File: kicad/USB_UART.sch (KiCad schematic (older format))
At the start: 10 parts, among them J3 USB-Micro, P5 CONN_1, P6 CONN_1, U3 CP210X

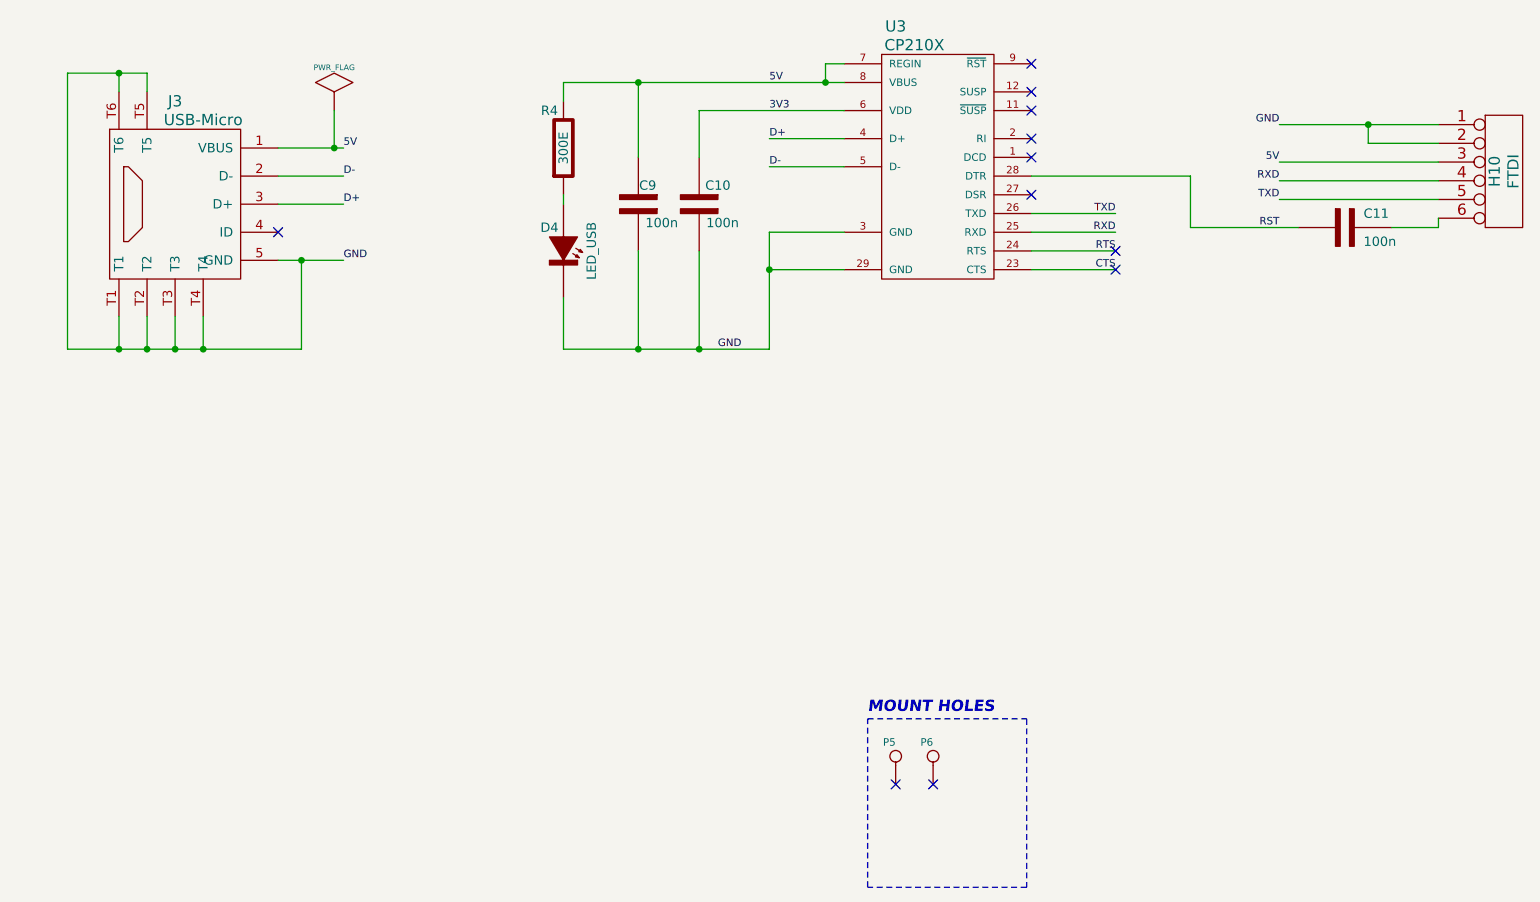
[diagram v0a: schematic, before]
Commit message: MAPone realigned headers to fit 0.1 breadboard
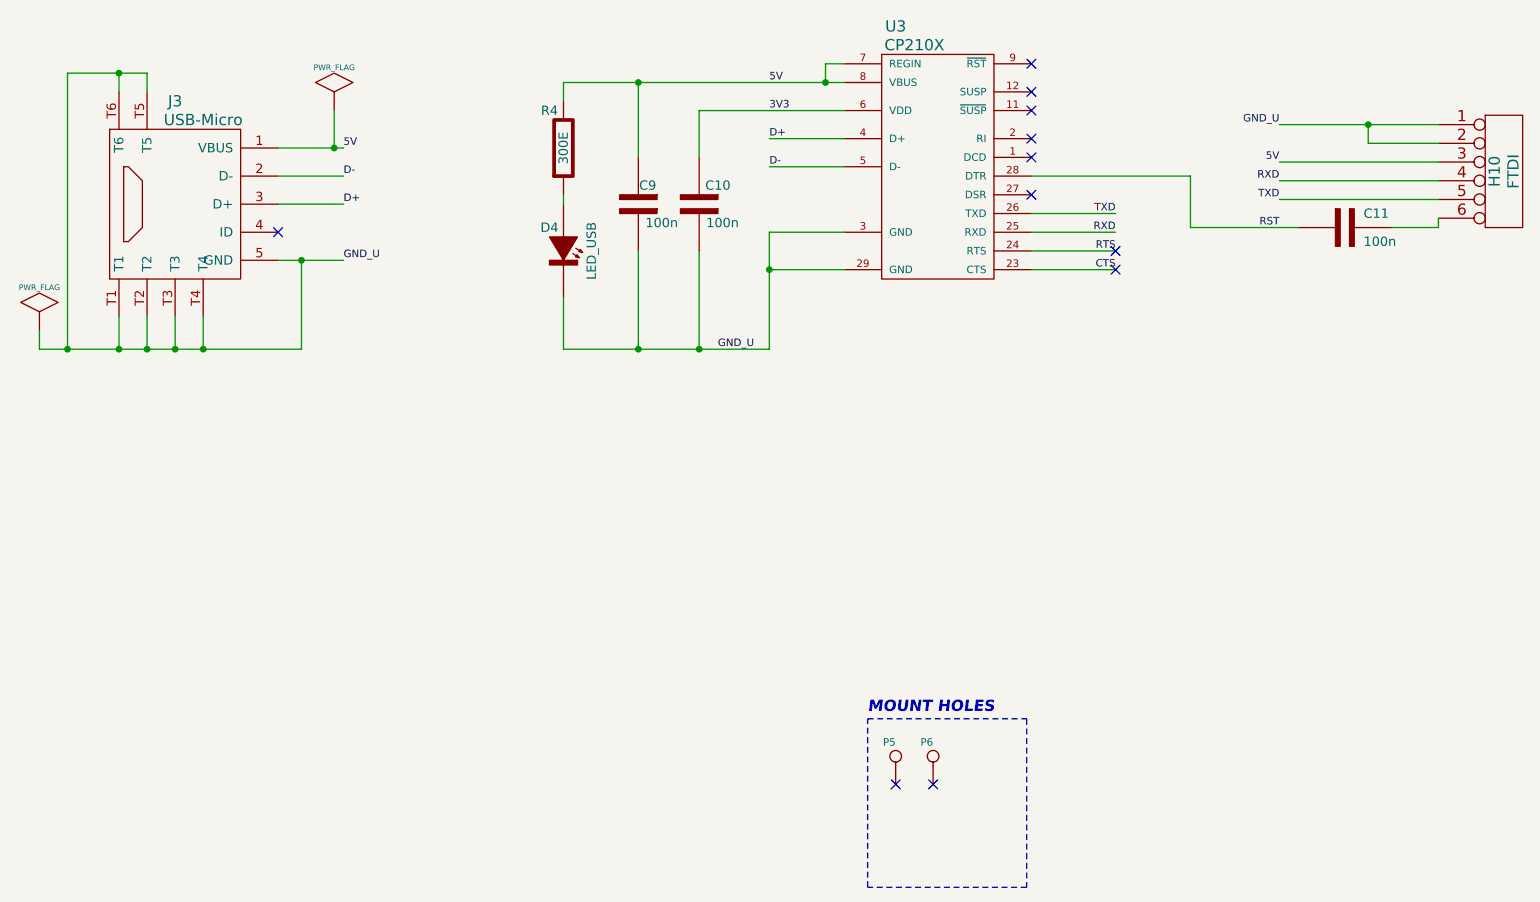
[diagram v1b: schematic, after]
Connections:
- net GND renamed GND_U
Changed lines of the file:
@@
 D-
 Text Label 5050 4550 0    40   ~ 0
-GND
+GND_U
 Text Label 7175 4125 2    40   ~ 0
 CTS
@@
 NoConn ~ 2700 3925
 Text Label 3050 4075 0    40   ~ 0
-GND
+GND_U
 $Comp
 L C_CPL C10
@@
 	1850 4375 1850 4550
 Wire Wire Line
-	1575 4550 2825 4550
+	1425 4550 2825 4550
 Wire Wire Line
 	2825 4550 2825 4075
@@
 $EndComp
 Text Label 8050 3350 2    40   ~ 0
-GND
+GND_U
 Text Label 8050 3750 2    40   ~ 0
 TXD
@@
 NoConn ~ 6000 6875
 NoConn ~ 6200 6875
+$Comp
+L PWR_FLAG #FLG013
+U 1 1 547CA2D7
+P 1425 4450
+F 0 "#FLG013" H 1425 4720 30  0001 C CNN
+F 1 "PWR_FLAG" H 1425 4680 30  0000 C CNN
+F 2 "" H 1425 4450 60  0000 C CNN
+F 3 "" H 1425 4450 60  0000 C CNN
+	1    1425 4450
+	1    0    0    -1
+$EndComp
+Wire Wire Line
+	1425 4550 1425 4450
+Connection ~ 1575 4550
 $EndSCHEMATC

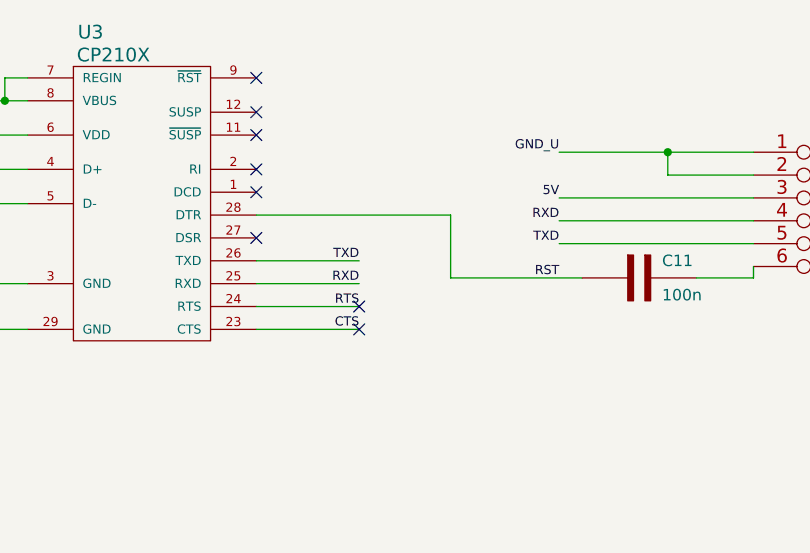
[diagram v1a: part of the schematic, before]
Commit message: MAPone made MAPusart smaller
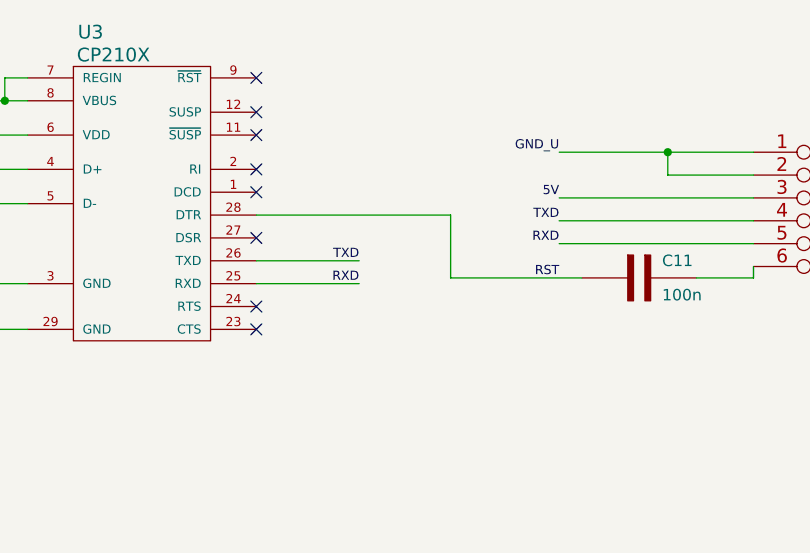
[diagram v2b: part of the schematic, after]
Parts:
- D4: footprint MAPone.pretty:LED-3MM -> MAPone.pretty:LED-0805
- H10: footprint MAPone.pretty:Header_FTDI -> MAPone.pretty:Socket_Strip_Angled_1x06
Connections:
- net RXD: now also H10.5; no longer H10.4
- net TXD: now also H10.4; no longer H10.5
- net CTS: no longer names the net of U3.23 (CTS)
- net RTS: no longer names the net of U3.24 (RTS)
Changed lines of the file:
@@
 Text Label 5050 4550 0    40   ~ 0
 GND_U
-Text Label 7175 4125 2    40   ~ 0
-CTS
-Text Label 7175 4025 2    40   ~ 0
-RTS
 Text Label 7175 3925 2    40   ~ 0
 RXD
@@
 Connection ~ 5325 4125
 Wire Wire Line
-	6725 4125 7175 4125
-Wire Wire Line
-	6725 4025 7175 4025
-Wire Wire Line
 	6725 3925 7175 3925
 Wire Wire Line
@@
 F 0 "D4" V 4100 3950 50  0000 C CNN
 F 1 "LED_USB" H 4225 4175 50  0000 C CNN
-F 2 "MAPone.pretty:LED-3MM" H 4295 4025 60  0001 C CNN
+F 2 "MAPone.pretty:LED-0805" H 4295 4025 60  0001 C CNN
 F 3 "" H 4295 4025 60  0000 C CNN
 	1    4225 4025
@@
 F 0 "H10" V 9200 3600 60  0000 C CNN
 F 1 "FTDI" V 9300 3600 60  0000 C CNN
-F 2 "MAPone.pretty:Header_FTDI" H 9250 3600 60  0001 C CNN
+F 2 "MAPone.pretty:Socket_Strip_Angled_1x06" H 9250 3600 60  0001 C CNN
 F 3 "" H 9250 3600 60  0001 C CNN
 	1    9250 3600
@@
 Text Label 8050 3350 2    40   ~ 0
 GND_U
+Text Label 8050 3650 2    40   ~ 0
+TXD
 Text Label 8050 3750 2    40   ~ 0
-TXD
-Text Label 8050 3650 2    40   ~ 0
 RXD
-NoConn ~ 7175 4025
-NoConn ~ 7175 4125
 $Comp
 L PWR_FLAG #FLG012
@@
 	1425 4550 1425 4450
 Connection ~ 1575 4550
+NoConn ~ 6725 4025
+NoConn ~ 6725 4125
 $EndSCHEMATC

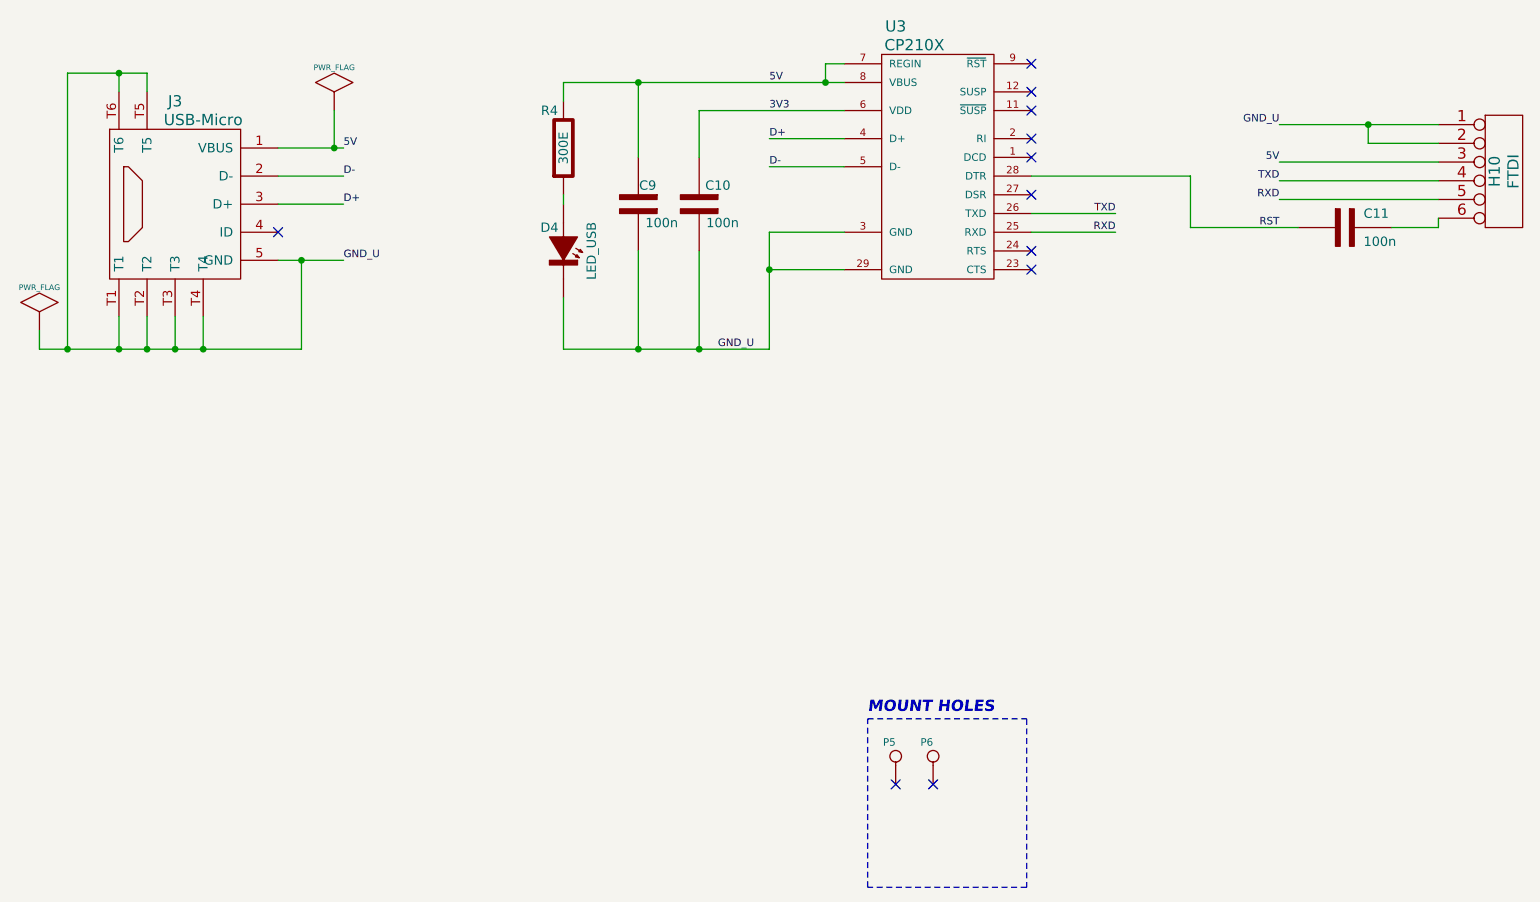
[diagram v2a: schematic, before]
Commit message: MAPone made MAPusart smaller
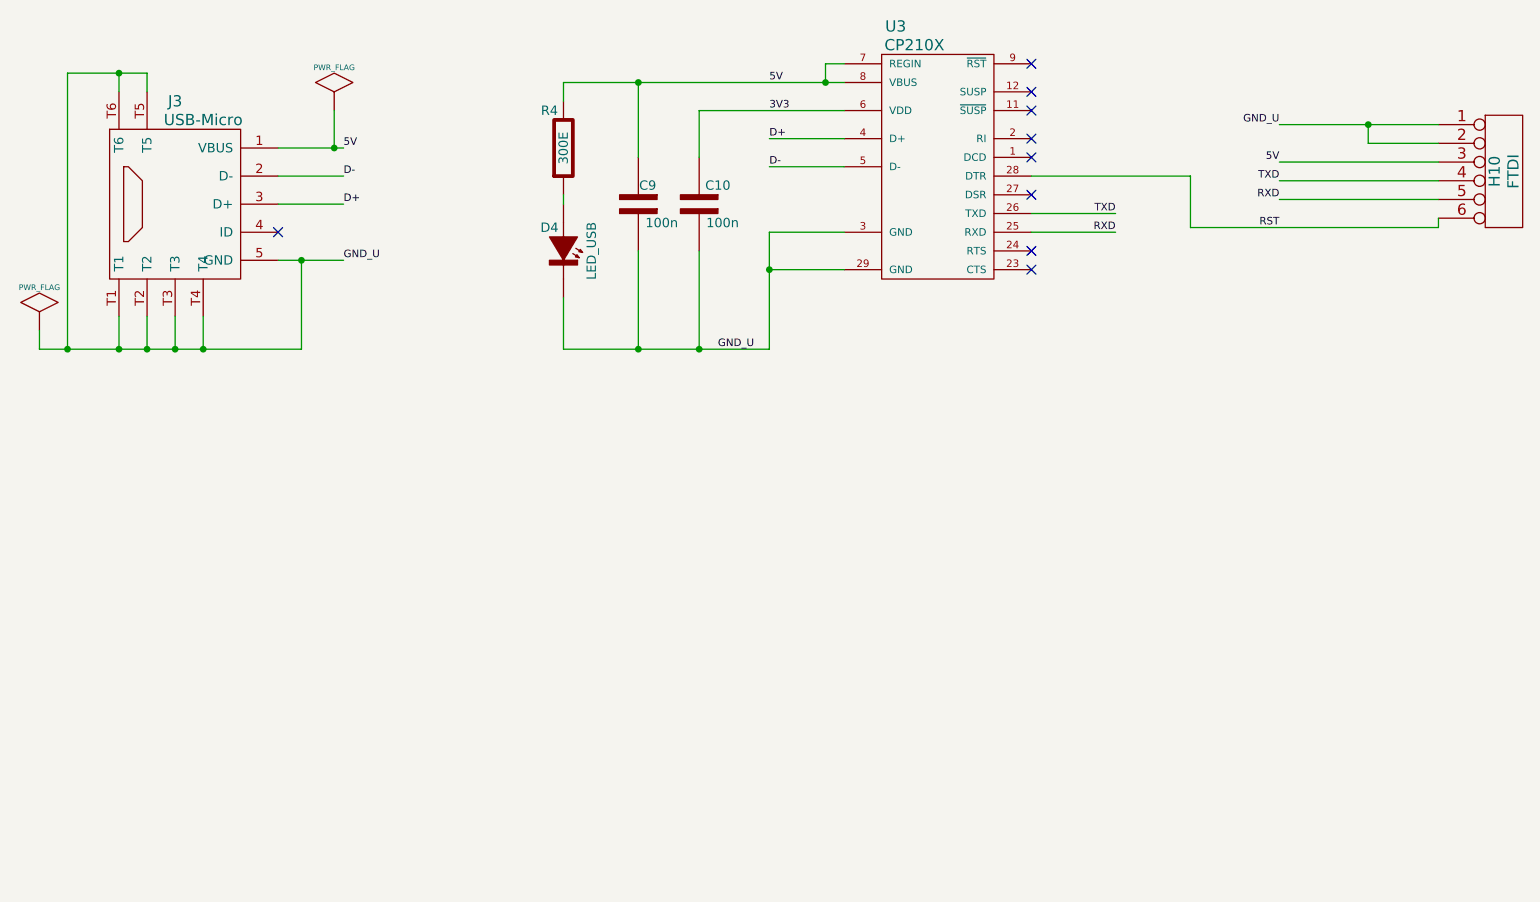
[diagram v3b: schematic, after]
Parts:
- removed C11: 100n, MAPone.pretty:C_0805_HandSoldering, symbol C_CPL
- removed P5, P6: CONN_1, MAPone.pretty:vite_3mm, symbol CONN_1
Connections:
- net RST: now also H10.6
- no-connect marks 11 -> 9
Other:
- note removed: "MOUNT HOLES"
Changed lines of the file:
@@
 	2000 3075 2000 3175
 Wire Wire Line
-	1850 4375 1850 4550
+	1850 4550 1850 4375
 Wire Wire Line
 	1425 4550 2825 4550
@@
 NoConn ~ 6725 3725
 Wire Wire Line
-	8650 3900 8900 3900
-Wire Wire Line
 	8900 3900 8900 3850
 Wire Wire Line
@@
 	8900 3750 8050 3750
 Wire Wire Line
-	7575 3900 8150 3900
+	7575 3900 8900 3900
 Text Label 8050 3550 2    40   ~ 0
 5V
 Text Label 8050 3900 2    40   ~ 0
 RST
-$Comp
-L C_CPL C11
-U 1 1 547B59C5
-P 8400 3900
-F 0 "C11" H 8500 3975 50  0000 L CNN
-F 1 "100n" H 8500 3825 50  0000 L CNN
-F 2 "MAPone.pretty:C_0805_HandSoldering" H 8400 3900 60  0001 C CNN
-F 3 "" H 8400 3900 60  0001 C CNN
-	1    8400 3900
-	1    0    0    -1
-$EndComp
 $Comp
 L CONN_6 H10
@@
 	7575 3625 7575 3900
 $Comp
-L CONN_1 P6
-U 1 1 547C2D6B
-P 6200 6725
-F 0 "P6" V 6275 6725 40  0000 L CNN
-F 1 "CONN_1" H 6200 6780 30  0001 C CNN
-F 2 "MAPone.pretty:vite_3mm" H 6200 6725 60  0001 C CNN
-F 3 "" H 6200 6725 60  0001 C CNN
-	1    6200 6725
-	0    -1   -1   0
-$EndComp
-$Comp
-L CONN_1 P5
-U 1 1 547C2D72
-P 6000 6725
-F 0 "P5" V 6075 6725 40  0000 L CNN
-F 1 "CONN_1" H 6000 6780 30  0001 C CNN
-F 2 "MAPone.pretty:vite_3mm" H 6000 6725 60  0001 C CNN
-F 3 "" H 6000 6725 60  0001 C CNN
-	1    6000 6725
-	0    -1   -1   0
-$EndComp
-Wire Notes Line
-	5850 7425 5850 6525
-Wire Notes Line
-	5850 6525 6700 6525
-Wire Notes Line
-	6700 6525 6700 7425
-Wire Notes Line
-	6700 7425 5850 7425
-Text Notes 5850 6500 0    60   Italic 12
-MOUNT HOLES
-NoConn ~ 6000 6875
-NoConn ~ 6200 6875
-$Comp
 L PWR_FLAG #FLG013
